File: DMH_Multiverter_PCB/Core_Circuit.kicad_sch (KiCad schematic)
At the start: 0 parts

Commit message: Finished schematic
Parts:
- added R1, R2, R4, R5: 100k, Resistor_THT:R_Axial_DIN0207_L6.3mm_D2.5mm_P7.62mm_Horizontal, symbol Device:R_US
- added R3, R6: 1k, Resistor_THT:R_Axial_DIN0207_L6.3mm_D2.5mm_P7.62mm_Horizontal, symbol Device:R_US
- added RV1, RV2: 100k, SynthStuff:Potentiometer_Alpha_RD901F-40-00D_Single_Vertical, symbol Device:R_Potentiometer_US
- added U1: TL072, Package_DIP:DIP-8_W7.62mm_Socket, symbol Amplifier_Operational:TL072
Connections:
- new net: R4.2, R5.1, U1.6 (-)
- new net: R2.2, R3.1, U1.1
- new net: R1.2, R2.1, U1.2 (-)
- new net: RV1.2, U1.3 (+)
- new net: RV2.2, U1.5 (+)
- new net: R5.2, R6.1, U1.7
- new net Att A Input: R1.1, RV1.3
- new net Att A Output: R3.2
- new net Att B Input: R4.1, RV2.3
- new net Att B Output: R6.2
- new net GND: RV1.1, RV2.1

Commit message: Adapted design to center detent pot P110KH-1F15
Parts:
- RV1, RV2: footprint SynthStuff:Potentiometer_Alpha_RD901F-40-00D_Single_Vertical -> SynthStuff:Potentiometer_TT_P110KH1
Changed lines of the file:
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@@
 			)
 		)
-		(property "Footprint" "SynthStuff:Potentiometer_Alpha_RD901F-40-00D_Single_Vertical"
+		(property "Footprint" "SynthStuff:Potentiometer_TT_P110KH1"
 			(at 44.45 44.45 0)
 			(effects
@@
 				)
 				(hide yes)
+			)
+		)
+		(property "Function" ""
+			(at 44.45 44.45 0)
+			(effects
+				(font
+					(size 1.27 1.27)
+				)
 			)
 		)
@@
 			)
 		)
-		(property "Footprint" "SynthStuff:Potentiometer_Alpha_RD901F-40-00D_Single_Vertical"
+		(property "Footprint" "SynthStuff:Potentiometer_TT_P110KH1"
 			(at 44.45 95.25 0)
 			(effects
@@
 			)
 		)
+		(property "Function" ""
+			(at 44.45 95.25 0)
+			(effects
+				(font
+					(size 1.27 1.27)
+				)
+			)
+		)

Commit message: Re-routing ongoing
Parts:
- removed R1, R4: 100k, Resistor_THT:R_Axial_DIN0207_L6.3mm_D2.5mm_P7.62mm_Horizontal, symbol Device:R_US
- added RV3, RV4: 50k, Potentiometer_THT:Potentiometer_Bourns_3296W_Vertical, symbol Device:R_Potentiometer_US
- R2, R5: value 100k -> 33k
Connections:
- net Att A Input: now also RV3.1
- net Att B Input: now also RV4.1
- net at R5.1, U1.6 (-): now also RV4.2, RV4.3
- net at R2.1, U1.2 (-): now also RV3.2, RV3.3
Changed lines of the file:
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@@
+	)
+	(junction
+		(at 64.77 25.4)
+		(diameter 0)
+		(color 0 0 0 0)
 	)
 	(junction
@@
 	)
 	(junction
+		(at 64.77 76.2)
+		(diameter 0)
+		(color 0 0 0 0)
+	)
+	(junction
 		(at 44.45 35.56)
 		(diameter 0)
@@
 	(wire
 		(pts
+			(xy 57.15 76.2) (xy 64.77 76.2)
+		)
+		(stroke
+			(width 0)
+			(type default)
+		)
+	)
+	(wire
+		(pts
 			(xy 64.77 95.25) (xy 64.77 91.44)
 		)
@@
 	(wire
 		(pts
+			(xy 57.15 25.4) (xy 64.77 25.4)
+		)
+		(stroke
+			(width 0)
+			(type default)
+		)
+	)
+	(wire
+		(pts
 			(xy 64.77 44.45) (xy 64.77 40.64)
 		)
@@
 	(wire
 		(pts
+			(xy 57.15 82.55) (xy 57.15 76.2)
+		)
+		(stroke
+			(width 0)
+			(type default)
+		)
+	)
+	(wire
+		(pts
 			(xy 87.63 88.9) (xy 83.82 88.9)
+		)
+		(stroke
+			(width 0)
+			(type default)
+		)
+	)
+	(wire
+		(pts
+			(xy 57.15 31.75) (xy 57.15 25.4)
 		)
 		(stroke
@@
 			)
 			(justify left)
-		)
-	)
-	(symbol
-		(lib_id "Device:R_US")
-		(at 57.15 86.36 90)
-		(unit 1)
-		(exclude_from_sim no)
-		(in_bom yes)
-		(on_board yes)
-		(dnp no)
-		(fields_autoplaced yes)
-		(property "Reference" "R4"
-			(at 57.15 80.01 90)
-			(effects
-				(font
-					(size 1.27 1.27)
-				)
-			)
-		)
-		(property "Value" "100k"
-			(at 57.15 82.55 90)
-			(effects
-				(font
-					(size 1.27 1.27)
-				)
-			)
-		)
-		(property "Footprint" "Resistor_THT:R_Axial_DIN0207_L6.3mm_D2.5mm_P7.62mm_Horizontal"
-			(at 57.404 85.344 90)
-			(effects
-				(font
-					(size 1.27 1.27)
-				)
-				(hide yes)
-			)
-		)
-		(property "Datasheet" "~"
-			(at 57.15 86.36 0)
-			(effects
-				(font
-					(size 1.27 1.27)
-				)
-				(hide yes)
-			)
-		)
-		(property "Description" "Resistor, US symbol"
-			(at 57.15 86.36 0)
-			(effects
-				(font
-					(size 1.27 1.27)
-				)
-				(hide yes)
-			)
-		)
-		(pin "1"
-		)
-		(pin "2"
-		)
-		(instances
-			(project "DMH_Multiverter_PCB"
-				(path "/58f4306d-5387-4983-bb08-41a2313fd315/7ad2d702-dfb7-4d49-a82d-34430dd5948f"
-					(reference "R4")
-					(unit 1)
-				)
-			)
 		)
 	)
@@
 	)
 	(symbol
+		(lib_id "Device:R_Potentiometer_US")
+		(at 57.15 86.36 90)
+		(unit 1)
+		(exclude_from_sim no)
+		(in_bom yes)
+		(on_board yes)
+		(dnp no)
+		(property "Reference" "RV4"
+			(at 57.15 90.17 90)
+			(effects
+				(font
+					(size 1.27 1.27)
+				)
+			)
+		)
+		(property "Value" "50k"
+			(at 57.15 92.71 90)
+			(effects
+				(font
+					(size 1.27 1.27)
+				)
+			)
+		)
+		(property "Footprint" "Potentiometer_THT:Potentiometer_Bourns_3296W_Vertical"
+			(at 57.15 86.36 0)
+			(effects
+				(font
+					(size 1.27 1.27)
+				)
+				(hide yes)
+			)
+		)
+		(property "Datasheet" "~"
+			(at 57.15 86.36 0)
+			(effects
+				(font
+					(size 1.27 1.27)
+				)
+				(hide yes)
+			)
+		)
+		(property "Description" "Potentiometer, US symbol"
+			(at 57.15 86.36 0)
+			(effects
+				(font
+					(size 1.27 1.27)
+				)
+				(hide yes)
+			)
+		)
+		(pin "3"
+		)
+		(pin "2"
+		)
+		(pin "1"
+		)
+		(instances
+			(project "DMH_Multiverter_PCB"
+				(path "/58f4306d-5387-4983-bb08-41a2313fd315/7ad2d702-dfb7-4d49-a82d-34430dd5948f"
+					(reference "RV4")
+					(unit 1)
+				)
+			)
+		)
+	)
+	(symbol
+		(lib_id "Device:R_Potentiometer_US")
+		(at 57.15 35.56 90)
+		(unit 1)
+		(exclude_from_sim no)
+		(in_bom yes)
+		(on_board yes)
+		(dnp no)
+		(property "Reference" "RV3"
+			(at 57.15 39.37 90)
+			(effects
+				(font
+					(size 1.27 1.27)
+				)
+			)
+		)
+		(property "Value" "50k"
+			(at 57.15 41.91 90)
+			(effects
+				(font
+					(size 1.27 1.27)
+				)
+			)
+		)
+		(property "Footprint" "Potentiometer_THT:Potentiometer_Bourns_3296W_Vertical"
+			(at 57.15 35.56 0)
+			(effects
+				(font
+					(size 1.27 1.27)
+				)
+				(hide yes)
+			)
+		)
+		(property "Datasheet" "~"
+			(at 57.15 35.56 0)
+			(effects
+				(font
+					(size 1.27 1.27)
+				)
+				(hide yes)
+			)
+		)
+		(property "Description" "Potentiometer, US symbol"
+			(at 57.15 35.56 0)
+			(effects
+				(font
+					(size 1.27 1.27)
+				)
+				(hide yes)
+			)
+		)
+		(pin "3"
+		)
+		(pin "2"
+		)
+		(pin "1"
+		)
+		(instances
+			(project ""
+				(path "/58f4306d-5387-4983-bb08-41a2313fd315/7ad2d702-dfb7-4d49-a82d-34430dd5948f"
+					(reference "RV3")
+					(unit 1)
+				)
+			)
+		)
+	)
+	(symbol
 		(lib_id "Amplifier_Operational:TL072")
 		(at 76.2 38.1 0)
@@
 	(symbol
 		(lib_id "Device:R_US")
-		(at 57.15 35.56 90)
-		(unit 1)
-		(exclude_from_sim no)
-		(in_bom yes)
-		(on_board yes)
-		(dnp no)
-		(fields_autoplaced yes)
-		(property "Reference" "R1"
-			(at 57.15 29.21 90)
-			(effects
-				(font
-					(size 1.27 1.27)
-				)
-			)
-		)
-		(property "Value" "100k"
-			(at 57.15 31.75 90)
-			(effects
-				(font
-					(size 1.27 1.27)
-				)
-			)
-		)
-		(property "Footprint" "Resistor_THT:R_Axial_DIN0207_L6.3mm_D2.5mm_P7.62mm_Horizontal"
-			(at 57.404 34.544 90)
-			(effects
-				(font
-					(size 1.27 1.27)
-				)
-				(hide yes)
-			)
-		)
-		(property "Datasheet" "~"
-			(at 57.15 35.56 0)
-			(effects
-				(font
-					(size 1.27 1.27)
-				)
-				(hide yes)
-			)
-		)
-		(property "Description" "Resistor, US symbol"
-			(at 57.15 35.56 0)
-			(effects
-				(font
-					(size 1.27 1.27)
-				)
-				(hide yes)
-			)
-		)
-		(pin "1"
-		)
-		(pin "2"
-		)
-		(instances
-			(project ""
-				(path "/58f4306d-5387-4983-bb08-41a2313fd315/7ad2d702-dfb7-4d49-a82d-34430dd5948f"
-					(reference "R1")
-					(unit 1)
-				)
-			)
-		)
-	)
-	(symbol
-		(lib_id "Device:R_US")
 		(at 95.25 38.1 90)
 		(unit 1)
@@
 			)
 		)
-		(property "Value" "100k"
+		(property "Value" "33k"
 			(at 76.2 72.39 90)
 			(effects
@@
 			)
 		)
-		(property "Value" "100k"
+		(property "Value" "33k"
 			(at 76.2 21.59 90)
 			(effects

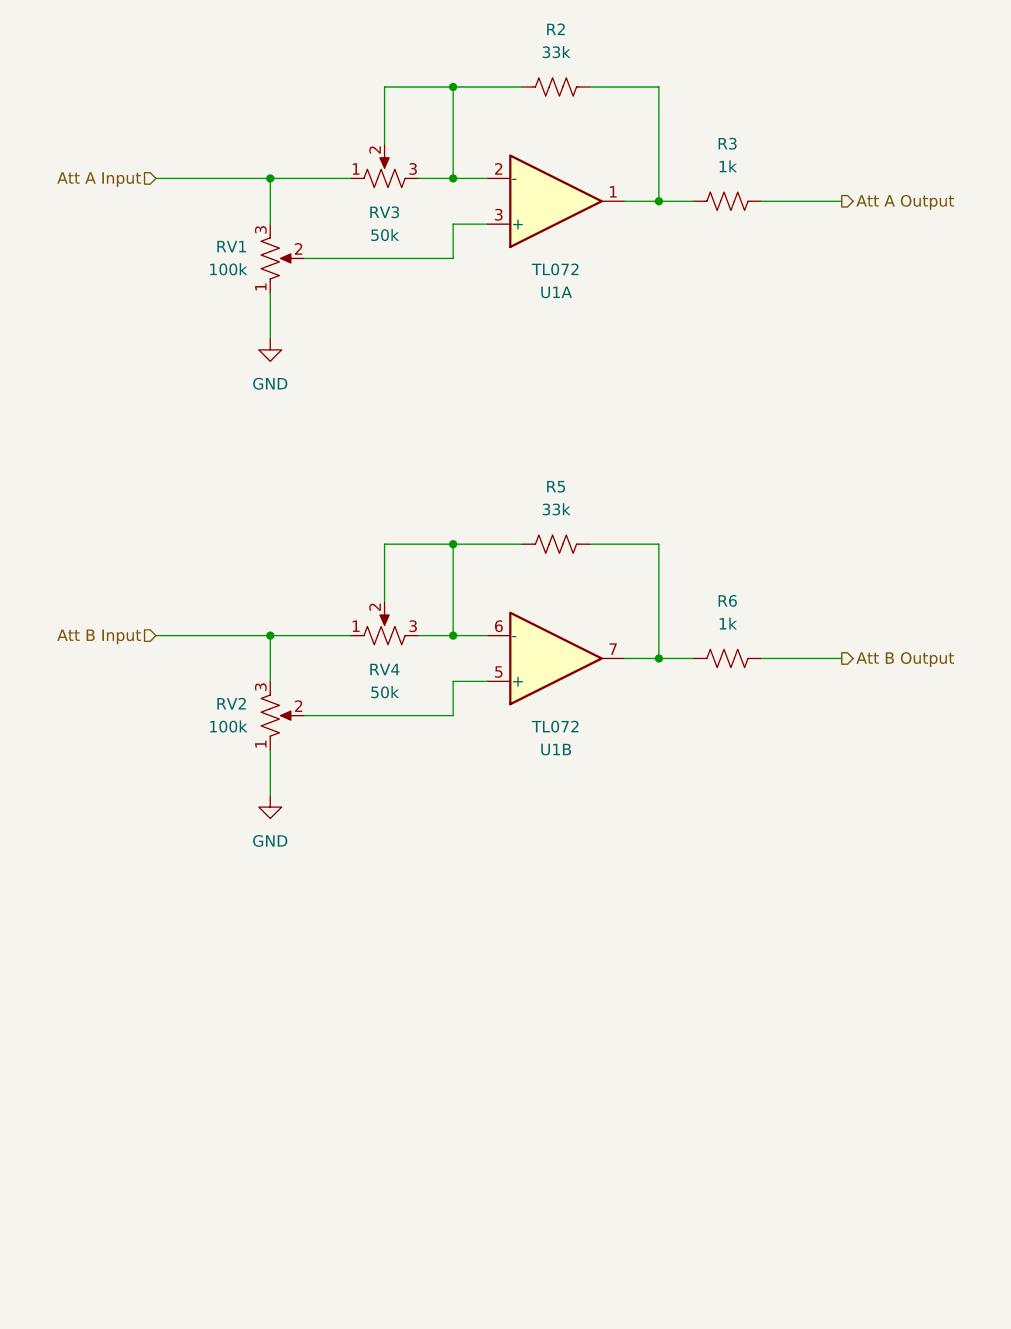
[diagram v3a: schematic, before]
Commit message: Testing out CV offset output feature
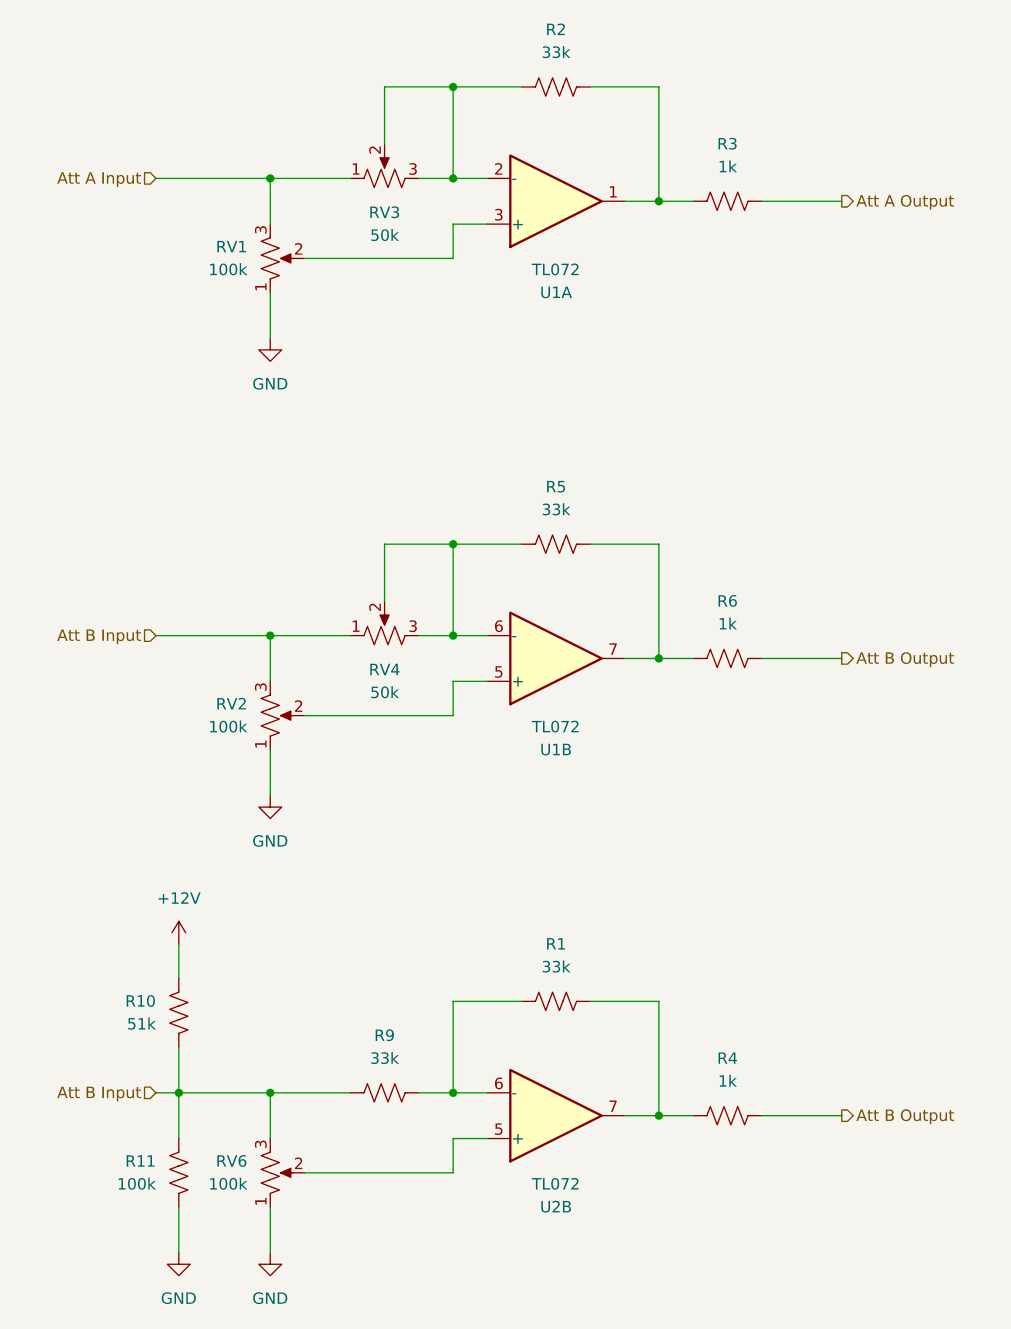
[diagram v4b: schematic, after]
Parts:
- added R1, R9: 33k, Resistor_THT:R_Axial_DIN0207_L6.3mm_D2.5mm_P7.62mm_Horizontal, symbol Device:R_US
- added R10: 51k, Resistor_THT:R_Axial_DIN0207_L6.3mm_D2.5mm_P7.62mm_Horizontal, symbol Device:R_US
- added R11: 100k, Resistor_THT:R_Axial_DIN0207_L6.3mm_D2.5mm_P7.62mm_Horizontal, symbol Device:R_US
- added R4: 1k, Resistor_THT:R_Axial_DIN0207_L6.3mm_D2.5mm_P7.62mm_Horizontal, symbol Device:R_US
- added RV6: 100k, SynthStuff:Potentiometer_TT_P110KH1, symbol Device:R_Potentiometer_US
- added U2: TL072, Package_DIP:DIP-8_W7.62mm_Socket, symbol Amplifier_Operational:TL072
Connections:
- net Att B Input: now also R10.2, R11.1, R9.1, RV6.3
- net Att B Output: now also R4.2
- net GND: now also R11.2, RV6.1
- new net: RV6.2, U2.5 (+)
- new net: R1.1, R9.2, U2.6 (-)
- new net: R1.2, R4.1, U2.7
- new net +12V: R10.1

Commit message: Testing attenuverter calibration
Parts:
- removed R11: 100k, Resistor_THT:R_Axial_DIN0207_L6.3mm_D2.5mm_P7.62mm_Horizontal, symbol Device:R_US
- added D3: ZPD5V1, Diode_THT:D_DO-35_SOD27_P7.62mm_Horizontal, symbol Diode:ZPDxx
- R10: value 51k -> 10k
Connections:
- net Att B Input: now also D3.1 (K)
- net GND: now also D3.2 (A)
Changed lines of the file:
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@@
-	)
-	(symbol
-		(lib_id "Device:R_US")
-		(at 34.29 146.05 0)
-		(mirror y)
-		(unit 1)
-		(exclude_from_sim no)
-		(in_bom yes)
-		(on_board yes)
-		(dnp no)
-		(property "Reference" "R11"
-			(at 31.75 144.7799 0)
-			(effects
-				(font
-					(size 1.27 1.27)
-				)
-				(justify left)
-			)
-		)
-		(property "Value" "100k"
-			(at 31.75 147.3199 0)
-			(effects
-				(font
-					(size 1.27 1.27)
-				)
-				(justify left)
-			)
-		)
-		(property "Footprint" "Resistor_THT:R_Axial_DIN0207_L6.3mm_D2.5mm_P7.62mm_Horizontal"
-			(at 33.274 146.304 90)
-			(effects
-				(font
-					(size 1.27 1.27)
-				)
-				(hide yes)
-			)
-		)
-		(property "Datasheet" "~"
-			(at 34.29 146.05 0)
-			(effects
-				(font
-					(size 1.27 1.27)
-				)
-				(hide yes)
-			)
-		)
-		(property "Description" "Resistor, US symbol"
-			(at 34.29 146.05 0)
-			(effects
-				(font
-					(size 1.27 1.27)
-				)
-				(hide yes)
-			)
-		)
-		(pin "1"
-		)
-		(pin "2"
-		)
-		(instances
-			(project "DMH_Multiverter_PCB"
-				(path "/58f4306d-5387-4983-bb08-41a2313fd315/7ad2d702-dfb7-4d49-a82d-34430dd5948f"
-					(reference "R11")
-					(unit 1)
-				)
-			)
-		)
 	)
 	(symbol
@@
 	)
 	(symbol
+		(lib_id "Diode:ZPDxx")
+		(at 34.29 146.05 270)
+		(unit 1)
+		(exclude_from_sim no)
+		(in_bom yes)
+		(on_board yes)
+		(dnp no)
+		(property "Reference" "D3"
+			(at 31.75 144.7799 90)
+			(effects
+				(font
+					(size 1.27 1.27)
+				)
+				(justify right)
+			)
+		)
+		(property "Value" "ZPD5V1"
+			(at 31.75 147.3199 90)
+			(effects
+				(font
+					(size 1.27 1.27)
+				)
+				(justify right)
+			)
+		)
+		(property "Footprint" "Diode_THT:D_DO-35_SOD27_P7.62mm_Horizontal"
+			(at 29.845 146.05 0)
+			(effects
+				(font
+					(size 1.27 1.27)
+				)
+				(hide yes)
+			)
+		)
+		(property "Datasheet" "http://diotec.com/tl_files/diotec/files/pdf/datasheets/zpd1"
+			(at 34.29 146.05 0)
+			(effects
+				(font
+					(size 1.27 1.27)
+				)
+				(hide yes)
+			)
+		)
+		(property "Description" "500mW Zener Diode, DO-35"
+			(at 34.29 146.05 0)
+			(effects
+				(font
+					(size 1.27 1.27)
+				)
+				(hide yes)
+			)
+		)
+		(property "Function" ""
+			(at 34.29 146.05 0)
+			(effects
+				(font
+					(size 1.27 1.27)
+				)
+			)
+		)
+		(pin "1"
+		)
+		(pin "2"
+		)
+		(instances
+			(project ""
+				(path "/58f4306d-5387-4983-bb08-41a2313fd315/7ad2d702-dfb7-4d49-a82d-34430dd5948f"
+					(reference "D3")
+					(unit 1)
+				)
+			)
+		)
+	)
+	(symbol
 		(lib_id "Device:R_US")
 		(at 95.25 139.7 90)
@@
 			)
 		)
-		(property "Value" "51k"
+		(property "Value" "10k"
 			(at 31.75 129.5399 0)
 			(effects
